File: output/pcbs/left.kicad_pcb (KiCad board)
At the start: 2 copper layers, 131.3 x 118.5 mm, 24 parts

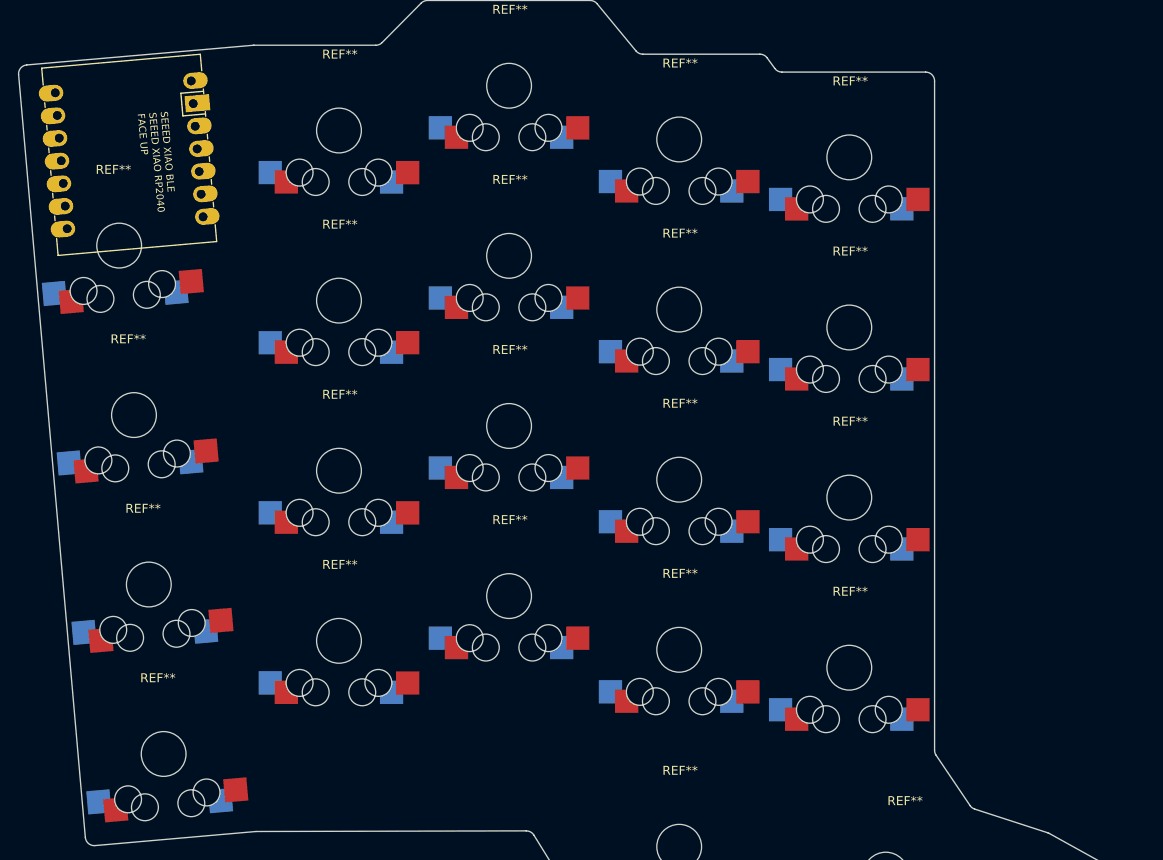
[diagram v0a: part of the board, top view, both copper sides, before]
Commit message: gonna change outline. wanted to commit before destroying it
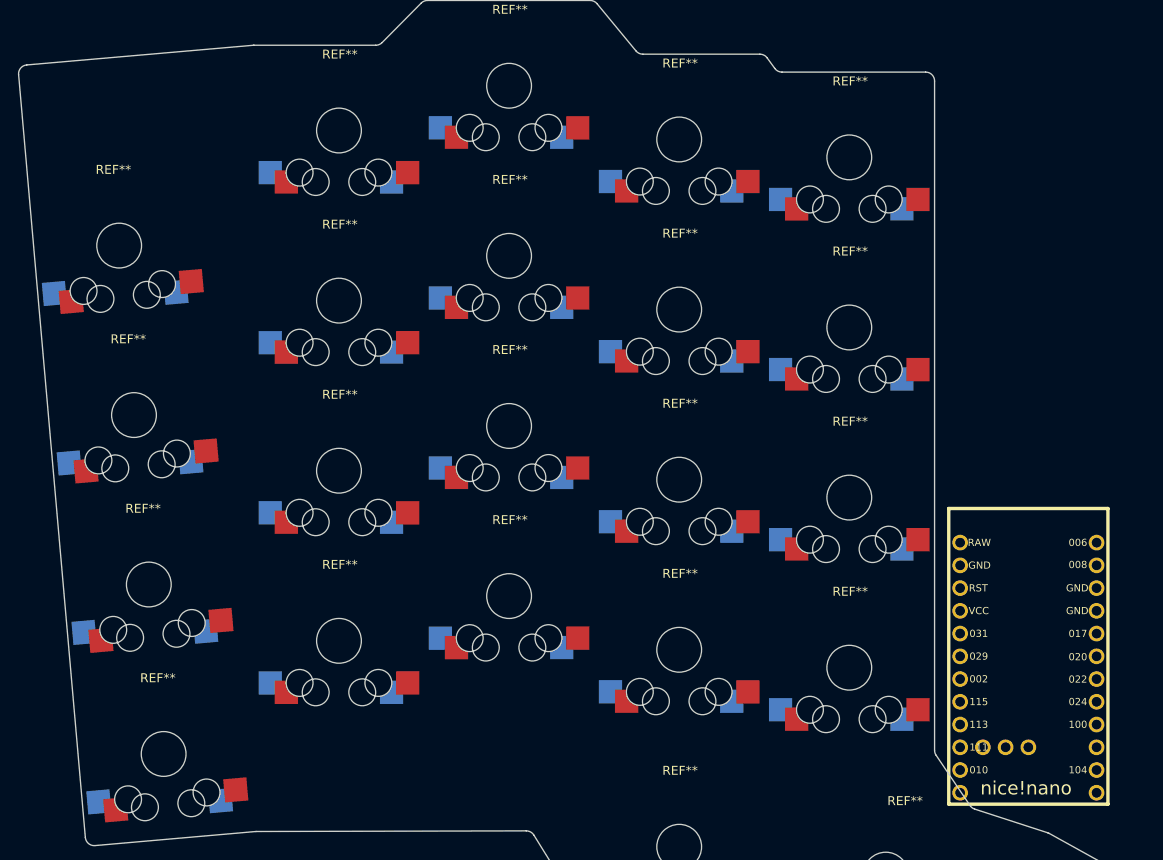
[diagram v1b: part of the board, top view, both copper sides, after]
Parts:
- MCU1: value (none) -> nice_nano; footprint xiao-ble -> nice_nano
- moved MCU1 115.6 mm to (196.6, 90.4), turned to -90 degrees
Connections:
- net P0 renamed P006
- net P1 renamed P008
- net P10 renamed P104
- net P4 renamed P017
- net P5 renamed P020
- net P6 renamed P022
- net P7 renamed P024
- net P8 renamed P100
- net P9 renamed P011
- net VUSB renamed P010
- MCU1 pad 12: VCC -> P106
- MCU1 pad 13: GND -> P009
- MCU1 pad 3: P2 -> GND
- MCU1 pad 4: P3 -> GND

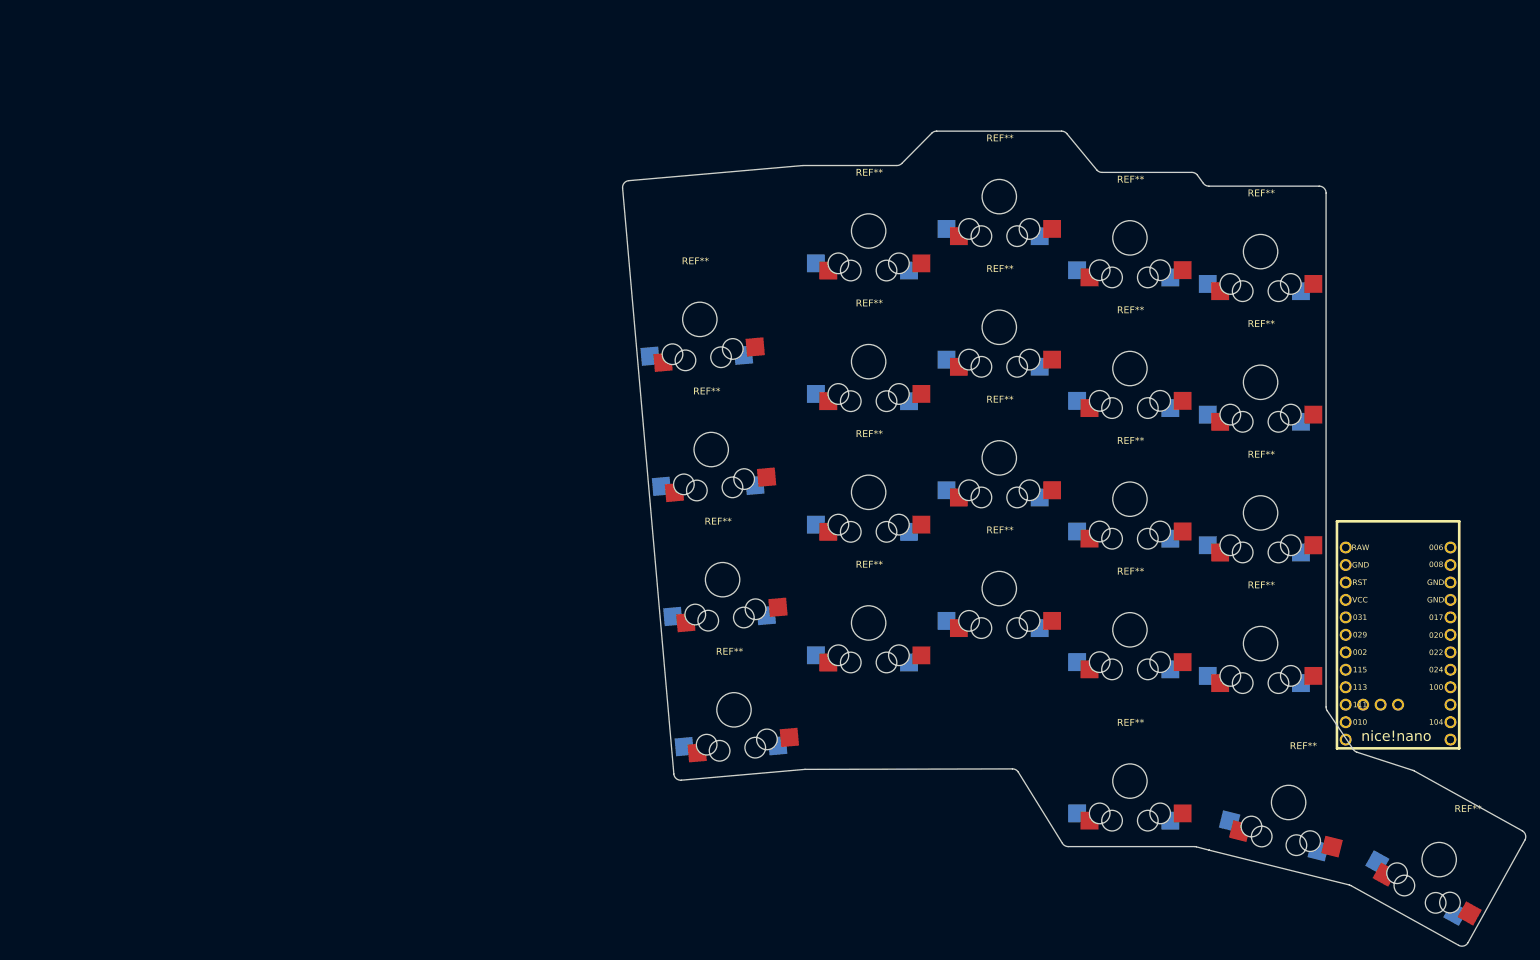
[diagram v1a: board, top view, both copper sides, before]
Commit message: super happy with how this is turning out
current todos:
 - Back lights
 - Battery
 - Name (FLotilla?)
 - inter-communications between halves
 - routing...
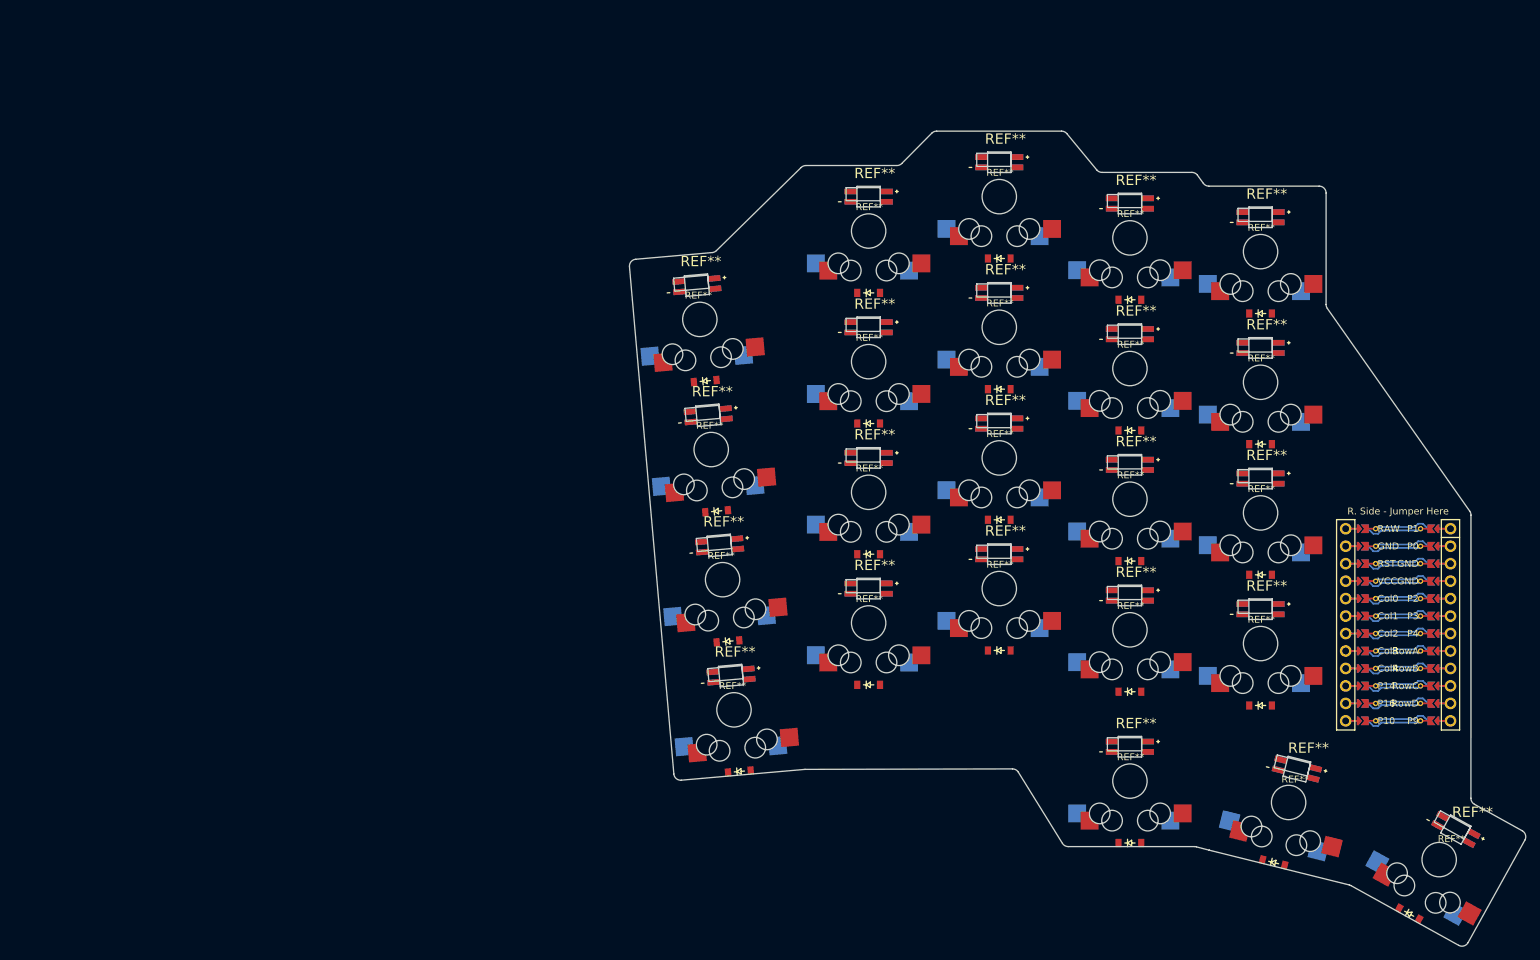
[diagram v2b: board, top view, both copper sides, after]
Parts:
- added D1: , ComboDiode, F.Cu at (100.8, 109.0)
- added D10: , ComboDiode, F.Cu at (138.6, 72.4)
- added D11: , ComboDiode, F.Cu at (138.6, 53.4)
- added D12: , ComboDiode, F.Cu at (138.6, 34.4)
- added D13: , ComboDiode, F.Cu at (157.6, 97.4)
- added D14: , ComboDiode, F.Cu at (157.6, 78.4)
- added D15: , ComboDiode, F.Cu at (157.6, 59.4)
- added D16: , ComboDiode, F.Cu at (157.6, 40.4)
- added D17: , ComboDiode, F.Cu at (176.6, 99.4)
- added D18: , ComboDiode, F.Cu at (176.6, 80.4)
- added D19: , ComboDiode, F.Cu at (176.6, 61.4)
- added D2: , ComboDiode, F.Cu at (99.1, 90.0)
- added D20: , ComboDiode, F.Cu at (176.6, 42.4)
- added D21: , ComboDiode, F.Cu at (157.6, 119.4)
- added D22: , ComboDiode, F.Cu at (178.5, 122.2)
- added D23: , ComboDiode, F.Cu at (198.2, 129.7)
- added D3: , ComboDiode, F.Cu at (97.5, 71.1)
- added D4: , ComboDiode, F.Cu at (95.8, 52.2)
- added D5: , ComboDiode, F.Cu at (119.6, 96.4)
- added D6: , ComboDiode, F.Cu at (119.6, 77.4)
- added D7: , ComboDiode, F.Cu at (119.6, 58.4)
- added D8: , ComboDiode, F.Cu at (119.6, 39.4)
- added D9: , ComboDiode, F.Cu at (138.6, 91.4)
- added REF**: LED_SK6812-E, LED_SK6812-E, F.Cu at (99.6, 95.0)
- added REF**: LED_SK6812-E, LED_SK6812-E, F.Cu at (97.9, 76.1)
- added REF**: LED_SK6812-E, LED_SK6812-E, F.Cu at (96.3, 57.2)
- added REF**: LED_SK6812-E, LED_SK6812-E, F.Cu at (94.6, 38.2)
- added REF**: LED_SK6812-E, LED_SK6812-E, F.Cu at (119.6, 82.4)
- added REF**: LED_SK6812-E, LED_SK6812-E, F.Cu at (119.6, 63.4)
- added REF**: LED_SK6812-E, LED_SK6812-E, F.Cu at (119.6, 44.4)
- added REF**: LED_SK6812-E, LED_SK6812-E, F.Cu at (119.6, 25.4)
- added REF**: LED_SK6812-E, LED_SK6812-E, F.Cu at (138.6, 77.4)
- added REF**: LED_SK6812-E, LED_SK6812-E, F.Cu at (138.6, 58.4)
- added REF**: LED_SK6812-E, LED_SK6812-E, F.Cu at (138.6, 39.4)
- added REF**: LED_SK6812-E, LED_SK6812-E, F.Cu at (138.6, 20.4)
- added REF**: LED_SK6812-E, LED_SK6812-E, F.Cu at (157.6, 83.4)
- added REF**: LED_SK6812-E, LED_SK6812-E, F.Cu at (157.6, 64.4)
- added REF**: LED_SK6812-E, LED_SK6812-E, F.Cu at (157.6, 45.4)
- added REF**: LED_SK6812-E, LED_SK6812-E, F.Cu at (157.6, 26.4)
- added REF**: LED_SK6812-E, LED_SK6812-E, F.Cu at (176.6, 85.4)
- added REF**: LED_SK6812-E, LED_SK6812-E, F.Cu at (176.6, 66.4)
- added REF**: LED_SK6812-E, LED_SK6812-E, F.Cu at (176.6, 47.4)
- added REF**: LED_SK6812-E, LED_SK6812-E, F.Cu at (176.6, 28.4)
- added REF**: LED_SK6812-E, LED_SK6812-E, F.Cu at (157.6, 105.4)
- added REF**: LED_SK6812-E, LED_SK6812-E, F.Cu at (181.9, 108.6)
- added REF**: LED_SK6812-E, LED_SK6812-E, F.Cu at (205.0, 117.4)
- MCU1: value nice_nano -> (none)
- REF** (x23): value ks27 -> k27
- moved MCU1 4.00 mm to (196.6, 86.4), turned to 0 degrees
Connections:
- net P002 renamed MCU1_18
- net P006 renamed MCU1_1
- net P008 renamed MCU1_2
- net P009 renamed MCU1_13
- net P010 renamed MCU1_14
- net P011 renamed MCU1_10
- net P017 renamed MCU1_5
- net P020 renamed MCU1_6
- net P022 renamed MCU1_7
- net P024 renamed MCU1_8
- net P029 renamed MCU1_19
- net P031 renamed MCU1_20
- net P100 renamed MCU1_9
- net P104 renamed MCU1_11
- net P106 renamed MCU1_12
- net P111 renamed MCU1_15
- net P113 renamed MCU1_16
- net P115 renamed MCU1_17
- net RAW renamed MCU1_24
- net RST renamed MCU1_22
- net VCC renamed MCU1_21
- MCU1 pad 23: GND -> MCU1_23
- MCU1 pad 3: GND -> MCU1_3
- MCU1 pad 4: GND -> MCU1_4
- REF** pad 1: (no net) -> Col0 (x4)
- REF** pad 2: (no net) -> pinky_bottom
- REF** pad 1: (no net) -> Col2 (x4)
- REF** pad 2: (no net) -> middle_home
- REF** pad 2: (no net) -> middle_top
- REF** pad 2: (no net) -> middle_number
- REF** pad 1: (no net) -> Col3 (x4)
- REF** pad 2: (no net) -> index_bottom
- REF** pad 2: (no net) -> index_home
- REF** pad 2: (no net) -> index_top
- REF** pad 2: (no net) -> index_number
- REF** pad 1: (no net) -> Col4 (x5)
- REF** pad 2: (no net) -> inner_bottom
- REF** pad 2: (no net) -> inner_home
- REF** pad 2: (no net) -> inner_top
- REF** pad 2: (no net) -> pinky_home
- REF** pad 2: (no net) -> inner_number
- REF** pad 2: (no net) -> near_thumb
- REF** pad 1: (no net) -> Col5 (x2)
- REF** pad 2: (no net) -> home_thumb
- REF** pad 2: (no net) -> far_thumb
- REF** pad 2: (no net) -> pinky_top
- REF** pad 2: (no net) -> pinky_number
- REF** pad 1: (no net) -> Col1 (x4)
- REF** pad 2: (no net) -> ring_bottom
- REF** pad 2: (no net) -> ring_home
- REF** pad 2: (no net) -> ring_top
- REF** pad 2: (no net) -> ring_number
- REF** pad 2: (no net) -> middle_bottom
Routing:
- net Col0: track 0.00 -> 122.0 mm
- net middle_home: track 0.00 -> 121.7 mm
- net inner_home: track 0.00 -> 50.9 mm
- net inner_top: track 0.00 -> 50.9 mm
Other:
- board size 131.3 x 118.5 mm -> 130.3 x 118.5 mm

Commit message: changed profile of mcu outline
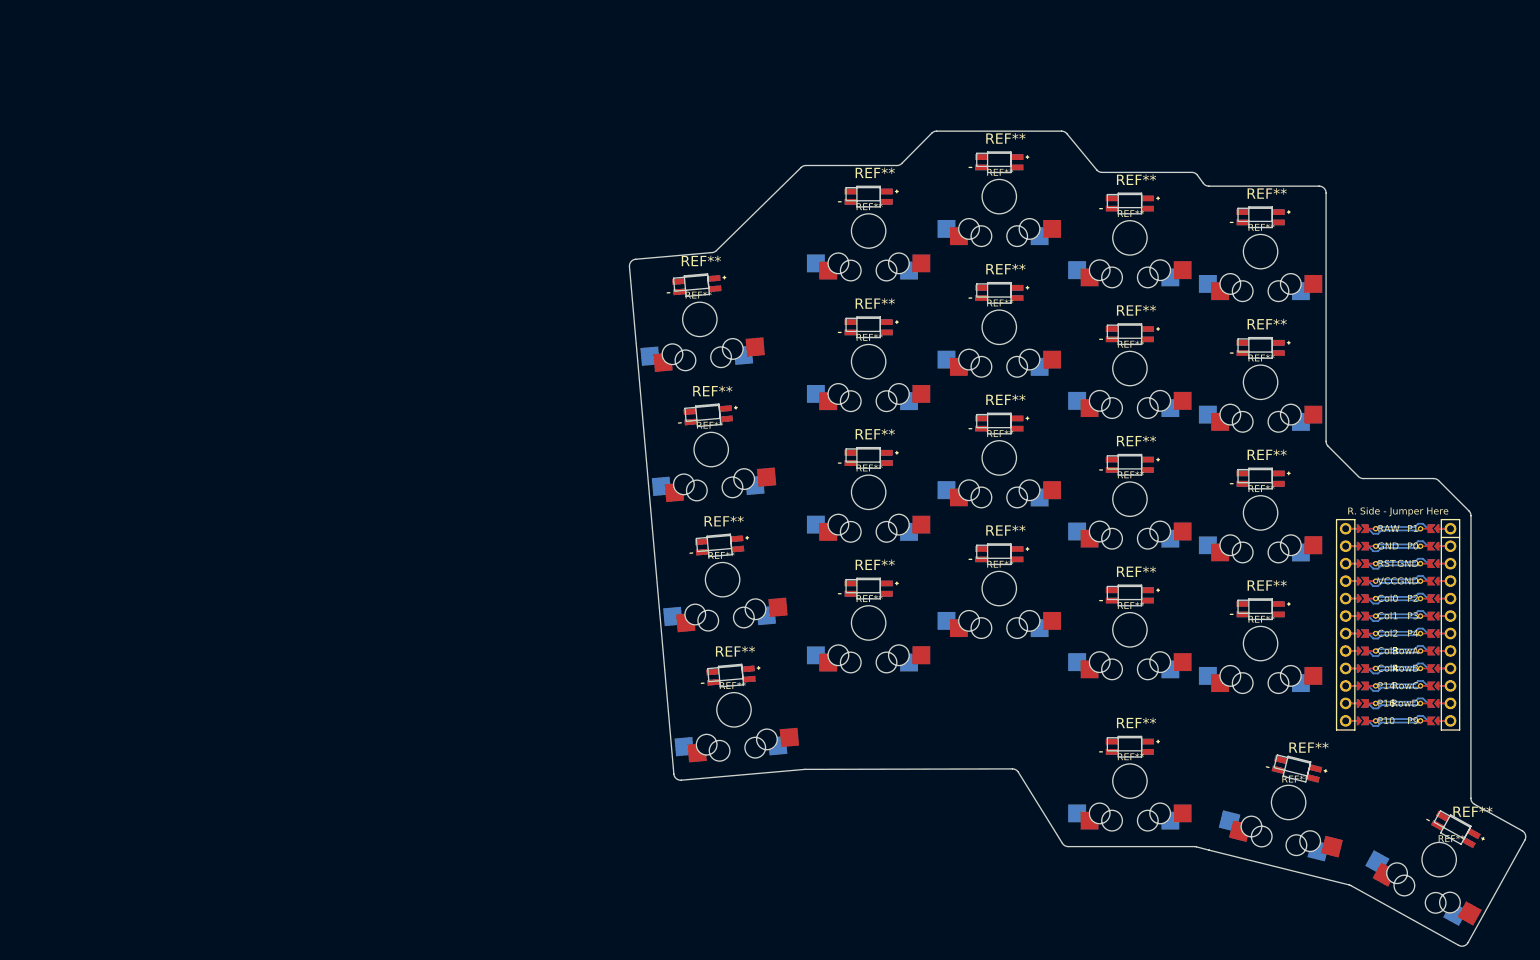
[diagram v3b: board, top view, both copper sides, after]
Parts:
- removed D1, D10, D11, D12, D13, D14, D15, D16, D17, D18, D19, D2, D20, D21, D22, D23, D3, D4, D5, D6, D7, D8, D9: , ComboDiode
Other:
- outline, holes or cut-outs redrawn
